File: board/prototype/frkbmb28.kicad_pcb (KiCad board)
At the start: 2 copper layers, 99.1 x 99.1 mm, 175 parts, among them P1 SHITTY_ADD_ON, P2 MCU_CONNECTOR, P3 SCL_JMP, P4 SDA_JMP, U1 IS31FL3741, U2 LIS2HH12

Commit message: ready to start laying out new board
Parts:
- removed R10, R11, R12, R13, R14, R15, R16, R17, R18, R19, R20, R21, R22, R23, R26, R27, R28, R29, R30, R31, R34, R35, R36, R37, R38, R39, R40, R41, R42, R43, R44, R45, R46, R47, R48, R6, R8: R, Resistors_SMD:R_0805_HandSoldering
- removed R7: 100k, Resistors_SMD:R_0603_HandSoldering
- removed R9: 20k, Resistors_SMD:R_0603_HandSoldering
- added C5: 220nF, Capacitors_SMD:C_0603_HandSoldering, F.Cu at (218.7, 121.0)
- added D118: LED, LEDs:LED_0805, F.Cu at (209.9, 163.7)
- added D119: LED, LEDs:LED_0805, F.Cu at (250.5, 127.8)
- added D120: LED, LEDs:LED_0805, F.Cu at (239.7, 161.1)
- added D121: LED, LEDs:LED_0805, F.Cu at (271.7, 127.8)
- added D122: LED, LEDs:LED_0805, F.Cu at (243.9, 155.5)
- added D123: LED, LEDs:LED_0805, F.Cu at (267.5, 133.3)
- added D124: LED, LEDs:LED_0805, F.Cu at (235.4, 166.6)
- added D125: LED, LEDs:LED_0805, F.Cu at (285.4, 116.7)
- added D126: LED, LEDs:LED_0805, F.Cu at (256.7, 144.4)
- added D127: LED, LEDs:LED_0805, F.Cu at (263.2, 127.8)
- added D128: LED, LEDs:LED_0805, F.Cu at (239.7, 150.0)
- added D129: LED, LEDs:LED_0805, F.Cu at (276.3, 122.2)
- added D130: LED, LEDs:LED_0805, F.Cu at (250.5, 138.9)
- added D131: LED, LEDs:LED_0805, F.Cu at (226.9, 162.1)
- added D132: LED, LEDs:LED_0805, F.Cu at (243.9, 144.4)
- added D133: LED, LEDs:LED_0805, F.Cu at (222.7, 167.6)
- added D134: LED, LEDs:LED_0805, F.Cu at (267.8, 122.2)
- added D135: LED, LEDs:LED_0805, F.Cu at (278.8, 111.1)
- added D136: LED, LEDs:LED_0805, F.Cu at (235.4, 155.5)
- added D137: LED, LEDs:LED_0805, F.Cu at (254.7, 133.3)
- added D138: LED, LEDs:LED_0805, F.Cu at (231.2, 161.0)
- added D139: LED, LEDs:LED_0805, F.Cu at (226.9, 167.6)
- added D140: LED, LEDs:LED_0805, F.Cu at (263.2, 133.3)
- added D141: LED, LEDs:LED_0805, F.Cu at (231.2, 166.5)
- added D142: LED, LEDs:LED_0805, F.Cu at (252.4, 144.4)
- added D143: LED, LEDs:LED_0805, F.Cu at (259.0, 138.9)
- added D144: LED, LEDs:LED_0805, F.Cu at (281.1, 116.7)
- C1: value 10uF -> 100nF; footprint SMD_Packages:SMD-1210_Pol -> Capacitors_SMD:C_0603_HandSoldering
- D1, D10, D100, D101, D102, D103, D104, D105, D106, D107, D108, D109, D11, D110, D111, D112, D113, D114, D115, D116, D117, D12, D13, D14, D15, D16, D17, D18, D19, D2, D20, D21, D22, D23, D24, D25, D26, D27, D28, D29, D3, D30, D31, D32, D33, D34, D35, D36, D37, D38, D39, D4, D40, D41, D42, D43, D44, D45, D46, D47, D48, D49, D5, D50, D51, D52, D53, D54, D55, D56, D57, D58, D59, D6, D60, D61, D62, D63, D64, D65, D66, D67, D68, D69, D7, D70, D71, D72, D73, D74, D75, D76, D77, D78, D79, D8, D80, D81, D82, D83, D84, D85, D86, D87, D88, D89, D9, D90, D91, D92, D93, D94, D95, D96, D97, D98, D99: value LED_ARGB -> LED; footprint frkbmb:0606_RGB_COMM_ANODE -> LEDs:LED_0805
- P2: footprint Pin_Headers:Pin_Header_Straight_1x18 -> Pin_Headers:Pin_Header_Straight_1x20
- R1: value R -> 4.7k; footprint Resistors_SMD:R_0805_HandSoldering -> Resistors_SMD:R_0603_HandSoldering
- R2, R3: value 1k -> 4.7k
- R5: value R -> 100k; footprint Resistors_SMD:R_0805_HandSoldering -> Resistors_SMD:R_0603_HandSoldering
- U1: value IS31FL3741 -> IS31FL3731; footprint frkbmb:IS31FL3741 -> frkbmb:IS31FL3731C
- U2: footprint frkbmb:LIS2HH12 -> frkbmb:LIS2HH12-NEW
- moved D19 255.0 mm to (276.9, 116.7)
- moved D21 251.9 mm to (283.1, 111.1)
- moved D22 241.6 mm to (272.0, 122.2)
- moved D101 237.2 mm to (270.3, 111.1)
- moved D110 236.0 mm to (268.4, 116.7)
- moved D109 235.3 mm to (259.0, 133.3)
- moved D73 234.5 mm to (261.8, 111.1)
- moved D20 234.1 mm to (239.7, 155.5)
- moved D112 233.3 mm to (274.6, 111.1)
- moved D100 233.0 mm to (259.3, 122.2)
- moved D83 229.8 mm to (259.9, 116.7)
- moved D23 228.8 mm to (248.2, 150.0)
- moved D78 228.1 mm to (272.6, 116.7)
- moved D96 225.1 mm to (267.5, 127.8)
- moved D91 224.9 mm to (246.2, 133.3)
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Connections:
- C1 pad 1: +3V3 -> GND
- C1 pad 2: GND -> Net-(C1-Pad2)
- C2 pad 1: +3V3 -> GND
- C2 pad 2: GND -> +3V3
- C3 pad 1: +3V3 -> GND
- C3 pad 2: GND -> +3V3
- D1 pad 1: /SW1 -> /CA1
- D1 pad 2: Net-(D1-Pad2) -> /CA2
- D10 pad 1: /SW1 -> /CB1
- D10 pad 2: Net-(D10-Pad2) -> /CB3
- D100 pad 1: /SW1 -> /CA7
- D100 pad 2: Net-(D100-Pad2) -> /CA4
- D101 pad 1: /SW2 -> /CA7
- D101 pad 2: Net-(D100-Pad2) -> /CA5
- D102 pad 1: /SW3 -> /CA7
- D102 pad 2: Net-(D100-Pad2) -> /CA6
- D103 pad 1: /SW4 -> /CA7
- D103 pad 2: Net-(D100-Pad2) -> /CA8
- D104 pad 1: /SW5 -> /CA7
- D104 pad 2: Net-(D100-Pad2) -> /CA9
- D105 pad 1: /SW6 -> /CB7
- D105 pad 2: Net-(D100-Pad2) -> /CB1
- D106 pad 1: /SW7 -> /CB7
- D106 pad 2: Net-(D100-Pad2) -> /CB2
- D107 pad 1: /SW8 -> /CB7
- D107 pad 2: Net-(D100-Pad2) -> /CB3
- D108 pad 1: /SW9 -> /CB7
- D108 pad 2: Net-(D100-Pad2) -> /CB4
- D109 pad 1: /SW1 -> /CB7
- D109 pad 2: Net-(D109-Pad2) -> /CB5
- D11 pad 1: /SW2 -> /CB1
- D11 pad 2: Net-(D10-Pad2) -> /CB4
- D110 pad 1: /SW2 -> /CB7
- D110 pad 2: Net-(D109-Pad2) -> /CB6
- D111 pad 1: /SW3 -> /CB7
- D111 pad 2: Net-(D109-Pad2) -> /CB8
- D112 pad 1: /SW4 -> /CB7
- D112 pad 2: Net-(D109-Pad2) -> /CB9
- D113 pad 1: /SW5 -> /CA8
- D113 pad 2: Net-(D109-Pad2) -> /CA1
- D114 pad 1: /SW6 -> /CA8
- D114 pad 2: Net-(D109-Pad2) -> /CA2
- D115 pad 1: /SW7 -> /CA8
- D115 pad 2: Net-(D109-Pad2) -> /CA3
- D116 pad 1: /SW8 -> /CA8
- D116 pad 2: Net-(D109-Pad2) -> /CA4
- D117 pad 1: /SW9 -> /CA8
- D117 pad 2: Net-(D109-Pad2) -> /CA5
- D12 pad 1: /SW3 -> /CB1
- D12 pad 2: Net-(D10-Pad2) -> /CB5
- D13 pad 1: /SW4 -> /CB1
- D13 pad 2: Net-(D10-Pad2) -> /CB6
- D14 pad 1: /SW5 -> /CB1
- D14 pad 2: Net-(D10-Pad2) -> /CB7
- D15 pad 1: /SW6 -> /CB1
- D15 pad 2: Net-(D10-Pad2) -> /CB8
- D16 pad 1: /SW7 -> /CB1
- D16 pad 2: Net-(D10-Pad2) -> /CB9
- D17 pad 1: /SW8 -> /CA2
- D17 pad 2: Net-(D10-Pad2) -> /CA1
- D18 pad 1: /SW9 -> /CA2
- D18 pad 2: Net-(D10-Pad2) -> /CA3
- D19 pad 1: /SW1 -> /CA2
- D19 pad 2: Net-(D19-Pad2) -> /CA4
- D2 pad 1: /SW2 -> /CA1
- D2 pad 2: Net-(D1-Pad2) -> /CA3
- D20 pad 1: /SW2 -> /CA2
- D20 pad 2: Net-(D19-Pad2) -> /CA5
- D21 pad 1: /SW3 -> /CA2
- D21 pad 2: Net-(D19-Pad2) -> /CA6
- D22 pad 1: /SW4 -> /CA2
- D22 pad 2: Net-(D19-Pad2) -> /CA7
- D23 pad 1: /SW5 -> /CA2
- D23 pad 2: Net-(D19-Pad2) -> /CA8
- D24 pad 1: /SW6 -> /CA2
- D24 pad 2: Net-(D19-Pad2) -> /CA9
- D25 pad 1: /SW7 -> /CB2
- D25 pad 2: Net-(D19-Pad2) -> /CB1
- D26 pad 1: /SW8 -> /CB2
- D26 pad 2: Net-(D19-Pad2) -> /CB3
- D27 pad 1: /SW9 -> /CB2
- D27 pad 2: Net-(D19-Pad2) -> /CB4
- D28 pad 1: /SW1 -> /CB2
- D28 pad 2: Net-(D28-Pad2) -> /CB5
- D29 pad 1: /SW2 -> /CB2
- D29 pad 2: Net-(D28-Pad2) -> /CB6
- D3 pad 1: /SW3 -> /CA1
- D3 pad 2: Net-(D1-Pad2) -> /CA4
- D30 pad 1: /SW3 -> /CB2
- D30 pad 2: Net-(D28-Pad2) -> /CB7
- D31 pad 1: /SW4 -> /CB2
- D31 pad 2: Net-(D28-Pad2) -> /CB8
- D32 pad 1: /SW5 -> /CB2
- D32 pad 2: Net-(D28-Pad2) -> /CB9
- D33 pad 1: /SW6 -> /CA3
- D33 pad 2: Net-(D28-Pad2) -> /CA1
- D34 pad 1: /SW7 -> /CA3
- D34 pad 2: Net-(D28-Pad2) -> /CA2
- D35 pad 1: /SW8 -> /CA3
- D35 pad 2: Net-(D28-Pad2) -> /CA4
- D36 pad 1: /SW9 -> /CA3
- D36 pad 2: Net-(D28-Pad2) -> /CA5
- D37 pad 1: /SW1 -> /CA3
- D37 pad 2: Net-(D37-Pad2) -> /CA6
- D38 pad 1: /SW2 -> /CA3
- D38 pad 2: Net-(D37-Pad2) -> /CA7
- D39 pad 1: /SW3 -> /CA3
- D39 pad 2: Net-(D37-Pad2) -> /CA8
- D4 pad 1: /SW4 -> /CA1
- D4 pad 2: Net-(D1-Pad2) -> /CA5
- D40 pad 1: /SW4 -> /CA3
- D40 pad 2: Net-(D37-Pad2) -> /CA9
- D41 pad 1: /SW5 -> /CB3
- D41 pad 2: Net-(D37-Pad2) -> /CB1
- D42 pad 1: /SW6 -> /CB3
- D42 pad 2: Net-(D37-Pad2) -> /CB2
- D43 pad 1: /SW7 -> /CB3
- D43 pad 2: Net-(D37-Pad2) -> /CB4
- D44 pad 1: /SW8 -> /CB3
- D44 pad 2: Net-(D37-Pad2) -> /CB5
- D45 pad 1: /SW9 -> /CB3
- D45 pad 2: Net-(D37-Pad2) -> /CB6
- D46 pad 1: /SW1 -> /CB3
- D46 pad 2: Net-(D46-Pad2) -> /CB7
- D47 pad 1: /SW2 -> /CB3
- D47 pad 2: Net-(D46-Pad2) -> /CB8
- D48 pad 1: /SW3 -> /CB3
- D48 pad 2: Net-(D46-Pad2) -> /CB9
- D49 pad 1: /SW4 -> /CA4
- D49 pad 2: Net-(D46-Pad2) -> /CA1
- D5 pad 1: /SW5 -> /CA1
- D5 pad 2: Net-(D1-Pad2) -> /CA6
- D50 pad 1: /SW5 -> /CA4
- D50 pad 2: Net-(D46-Pad2) -> /CA2
- D51 pad 1: /SW6 -> /CA4
- D51 pad 2: Net-(D46-Pad2) -> /CA3
- D52 pad 1: /SW7 -> /CA4
- D52 pad 2: Net-(D46-Pad2) -> /CA5
- D53 pad 1: /SW8 -> /CA4
- D53 pad 2: Net-(D46-Pad2) -> /CA6
- D54 pad 1: /SW9 -> /CA4
- D54 pad 2: Net-(D46-Pad2) -> /CA7
- D55 pad 1: /SW1 -> /CA4
- D55 pad 2: Net-(D55-Pad2) -> /CA8
- D56 pad 1: /SW2 -> /CA4
- D56 pad 2: Net-(D55-Pad2) -> /CA9
- D57 pad 1: /SW3 -> /CB4
- D57 pad 2: Net-(D55-Pad2) -> /CB1
- D58 pad 1: /SW4 -> /CB4
- D58 pad 2: Net-(D55-Pad2) -> /CB2
- D59 pad 1: /SW5 -> /CB4
- D59 pad 2: Net-(D55-Pad2) -> /CB3
- D6 pad 1: /SW6 -> /CA1
- D6 pad 2: Net-(D1-Pad2) -> /CA7
- D60 pad 1: /SW6 -> /CB4
- D60 pad 2: Net-(D55-Pad2) -> /CB5
- D61 pad 1: /SW7 -> /CB4
- D61 pad 2: Net-(D55-Pad2) -> /CB6
- D62 pad 1: /SW8 -> /CB4
- D62 pad 2: Net-(D55-Pad2) -> /CB7
- D63 pad 1: /SW9 -> /CB4
- D63 pad 2: Net-(D55-Pad2) -> /CB8
- D64 pad 1: /SW1 -> /CB4
- D64 pad 2: Net-(D64-Pad2) -> /CB9
- D65 pad 1: /SW2 -> /CA5
- D65 pad 2: Net-(D64-Pad2) -> /CA1
- D66 pad 1: /SW3 -> /CA5
- D66 pad 2: Net-(D64-Pad2) -> /CA2
- D67 pad 1: /SW4 -> /CA5
- D67 pad 2: Net-(D64-Pad2) -> /CA3
- D68 pad 1: /SW5 -> /CA5
- D68 pad 2: Net-(D64-Pad2) -> /CA4
- D69 pad 1: /SW6 -> /CA5
- D69 pad 2: Net-(D64-Pad2) -> /CA6
- D7 pad 1: /SW7 -> /CA1
- D7 pad 2: Net-(D1-Pad2) -> /CA8
- D70 pad 1: /SW7 -> /CA5
- D70 pad 2: Net-(D64-Pad2) -> /CA7
- D71 pad 1: /SW8 -> /CA5
- D71 pad 2: Net-(D64-Pad2) -> /CA8
- D72 pad 1: /SW9 -> /CA5
- D72 pad 2: Net-(D64-Pad2) -> /CA9
- D73 pad 1: /SW1 -> /CB5
- D73 pad 2: Net-(D73-Pad2) -> /CB1
- D74 pad 1: /SW2 -> /CB5
- D74 pad 2: Net-(D73-Pad2) -> /CB2
- D75 pad 1: /SW3 -> /CB5
- D75 pad 2: Net-(D73-Pad2) -> /CB3
- D76 pad 1: /SW4 -> /CB5
- D76 pad 2: Net-(D73-Pad2) -> /CB4
- D77 pad 1: /SW5 -> /CB5
- D77 pad 2: Net-(D73-Pad2) -> /CB6
- D78 pad 1: /SW6 -> /CB5
- D78 pad 2: Net-(D73-Pad2) -> /CB7
- D79 pad 1: /SW7 -> /CB5
- D79 pad 2: Net-(D73-Pad2) -> /CB8
- D8 pad 1: /SW8 -> /CA1
- D8 pad 2: Net-(D1-Pad2) -> /CA9
- D80 pad 1: /SW8 -> /CB5
- D80 pad 2: Net-(D73-Pad2) -> /CB9
- D81 pad 1: /SW9 -> /CA6
- D81 pad 2: Net-(D73-Pad2) -> /CA1
- D82 pad 1: /SW1 -> /CA6
- D82 pad 2: Net-(D82-Pad2) -> /CA2
- D83 pad 1: /SW2 -> /CA6
- D83 pad 2: Net-(D82-Pad2) -> /CA3
- D84 pad 1: /SW3 -> /CA6
- D84 pad 2: Net-(D82-Pad2) -> /CA4
- D85 pad 1: /SW4 -> /CA6
- D85 pad 2: Net-(D82-Pad2) -> /CA5
- D86 pad 1: /SW5 -> /CA6
- D86 pad 2: Net-(D82-Pad2) -> /CA7
- D87 pad 1: /SW6 -> /CA6
- D87 pad 2: Net-(D82-Pad2) -> /CA8
- D88 pad 1: /SW7 -> /CA6
- D88 pad 2: Net-(D82-Pad2) -> /CA9
- D89 pad 1: /SW8 -> /CB6
- D89 pad 2: Net-(D82-Pad2) -> /CB1
- D9 pad 1: /SW9 -> /CB1
- D9 pad 2: Net-(D1-Pad2) -> /CB2
- D90 pad 1: /SW9 -> /CB6
- D90 pad 2: Net-(D82-Pad2) -> /CB2
- D91 pad 1: /SW1 -> /CB6
- D91 pad 2: Net-(D91-Pad2) -> /CB3
- D92 pad 1: /SW2 -> /CB6
- D92 pad 2: Net-(D91-Pad2) -> /CB4
- D93 pad 1: /SW3 -> /CB6
- D93 pad 2: Net-(D91-Pad2) -> /CB5
- D94 pad 1: /SW4 -> /CB6
- D94 pad 2: Net-(D91-Pad2) -> /CB7
- D95 pad 1: /SW5 -> /CB6
- D95 pad 2: Net-(D91-Pad2) -> /CB8
- D96 pad 1: /SW6 -> /CB6
- D96 pad 2: Net-(D91-Pad2) -> /CB9
- D97 pad 1: /SW7 -> /CA7
- D97 pad 2: Net-(D91-Pad2) -> /CA1
- D98 pad 1: /SW8 -> /CA7
- D98 pad 2: Net-(D91-Pad2) -> /CA2
- D99 pad 1: /SW9 -> /CA7
- D99 pad 2: Net-(D91-Pad2) -> /CA3
- P2 pad 10: /SCL_ACC -> /AUD
- P2 pad 11: /SA0/SDo -> /SDA_ACC
- P2 pad 12: /CS -> /SCL_ACC
- P2 pad 13: /INT1 -> /SA0/SDo
- P2 pad 14: /INT2 -> /CS
- P2 pad 15: /SDA_SAO -> /INT1
- P2 pad 16: /SCL_SAO -> /INT2
- P2 pad 17: /GPIO1 -> /SDA_SAO
- P2 pad 18: /GPIO2 -> /SCL_SAO
- P2 pad 5: /SDA_MTX -> GND
- P2 pad 6: /SCL_MTX -> /SDA_MTX
- P2 pad 7: /INTB -> /SCL_MTX
- P2 pad 8: /SDB -> /INTB
- P2 pad 9: /SDA_ACC -> /SDB
- R1 pad 1: Net-(D1-Pad2) -> /INTB
- R1 pad 2: /CS1 -> +3V3
- R2 pad 1: +3V3 -> /SCL_MTX
- R2 pad 2: /SCL_MTX -> +3V3
- R3 pad 1: +3V3 -> /SDA_MTX
- R3 pad 2: /SDA_MTX -> +3V3
- R4 pad 1: +3V3 -> GND
- R4 pad 2: /SDB -> Net-(R4-Pad2)
- R5 pad 1: Net-(D1-Pad3) -> GND
- R5 pad 2: /CS2 -> Net-(R5-Pad2)
- U1 pad 1: /CS34 -> /CA9
- U1 pad 10: /SCL_MTX -> Net-(U1-Pad10)
- U1 pad 11: /SDB -> Net-(U1-Pad11)
- U1 pad 12: (no net) -> Net-(U1-Pad12)
- U1 pad 14: +3V3 -> Net-(U1-Pad14)
- U1 pad 15: +3V3 -> Net-(U1-Pad15)
- U1 pad 16: /SW1 -> Net-(C1-Pad2)
- U1 pad 17: /SW2 -> Net-(C5-Pad1)
- U1 pad 18: /SW3 -> GND
- U1 pad 19: /SW4 -> /SDA_MTX
- U1 pad 2: /CS35 -> +3V3
- U1 pad 20: /SW5 -> /SCL_MTX
- U1 pad 21: /SW6 -> /CA1
- U1 pad 22: /SW7 -> /CA2
- U1 pad 23: /SW8 -> /CA3
- U1 pad 24: /SW9 -> /CA4
- U1 pad 25: +3V3 -> /CA5
- U1 pad 26: /CS1 -> /CA6
- U1 pad 27: /CS2 -> /CA7
- U1 pad 28: /CS3 -> /CA8
- U1 pad 29: /CS4 -> GND
- U1 pad 3: /CS36 -> /SDB
- U1 pad 4: /CS37 -> /INTB
- U1 pad 5: /CS38 -> GND
- U1 pad 6: /CS39 -> Net-(R5-Pad2)
- U1 pad 7: /INTB -> Net-(U1-Pad7)
- U1 pad 8: GND -> Net-(U1-Pad8)
- U1 pad 9: /SDA_MTX -> Net-(U1-Pad9)
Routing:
- net Net-(D109-Pad4): track 46.2 -> 0.00 mm, vias 9 -> 0
- net Net-(D100-Pad4): track 45.9 -> 0.00 mm, vias 9 -> 0
- net Net-(D91-Pad4): track 45.8 -> 0.00 mm, vias 9 -> 0
- net Net-(D82-Pad4): track 45.6 -> 0.00 mm, vias 9 -> 0
- net Net-(D73-Pad4): track 45.6 -> 0.00 mm, vias 9 -> 0
- net Net-(D64-Pad4): track 45.3 -> 0.00 mm, vias 9 -> 0
- net Net-(D55-Pad4): track 45.1 -> 0.00 mm, vias 9 -> 0
- net Net-(D46-Pad4): track 45.0 -> 0.00 mm, vias 9 -> 0
- net Net-(D37-Pad4): track 44.8 -> 0.00 mm, vias 9 -> 0
- net Net-(D28-Pad4): track 44.7 -> 0.00 mm, vias 9 -> 0
- net Net-(D1-Pad4): track 44.6 -> 0.00 mm, vias 9 -> 0
- net Net-(D19-Pad4): track 44.5 -> 0.00 mm, vias 9 -> 0
- net Net-(D10-Pad4): track 44.4 -> 0.00 mm, vias 9 -> 0
- net /SW7: track 39.8 -> 0.00 mm
- net /SW9: track 39.6 -> 0.00 mm
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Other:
- board outline removed
- net class Default: trace_width 0.2 -> 0.127
- rule pad_to_mask_clearance: 0.2 -> 0
- rule trace_min: 0.2 -> 0.127
- rule via_min_size: 0.45 -> 0.4

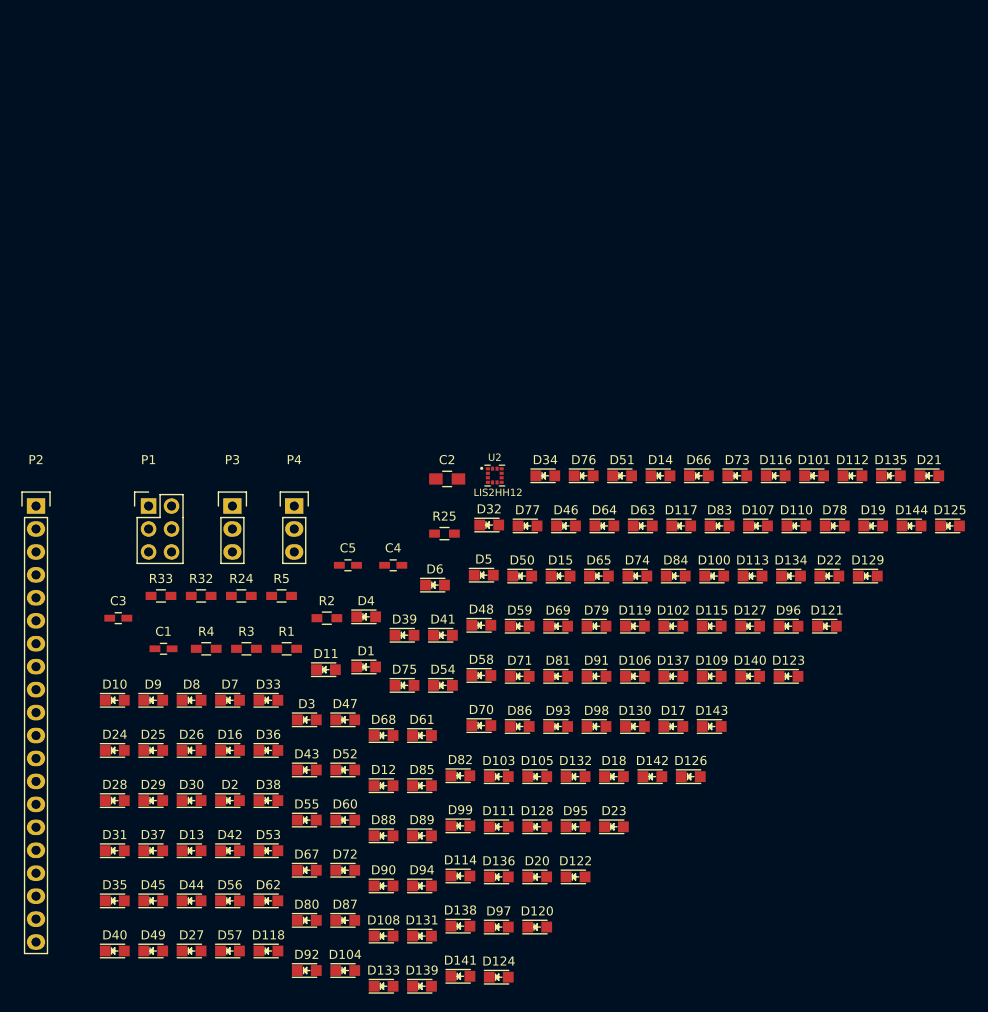
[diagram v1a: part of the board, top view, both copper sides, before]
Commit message: organized the LEDs on the prototype
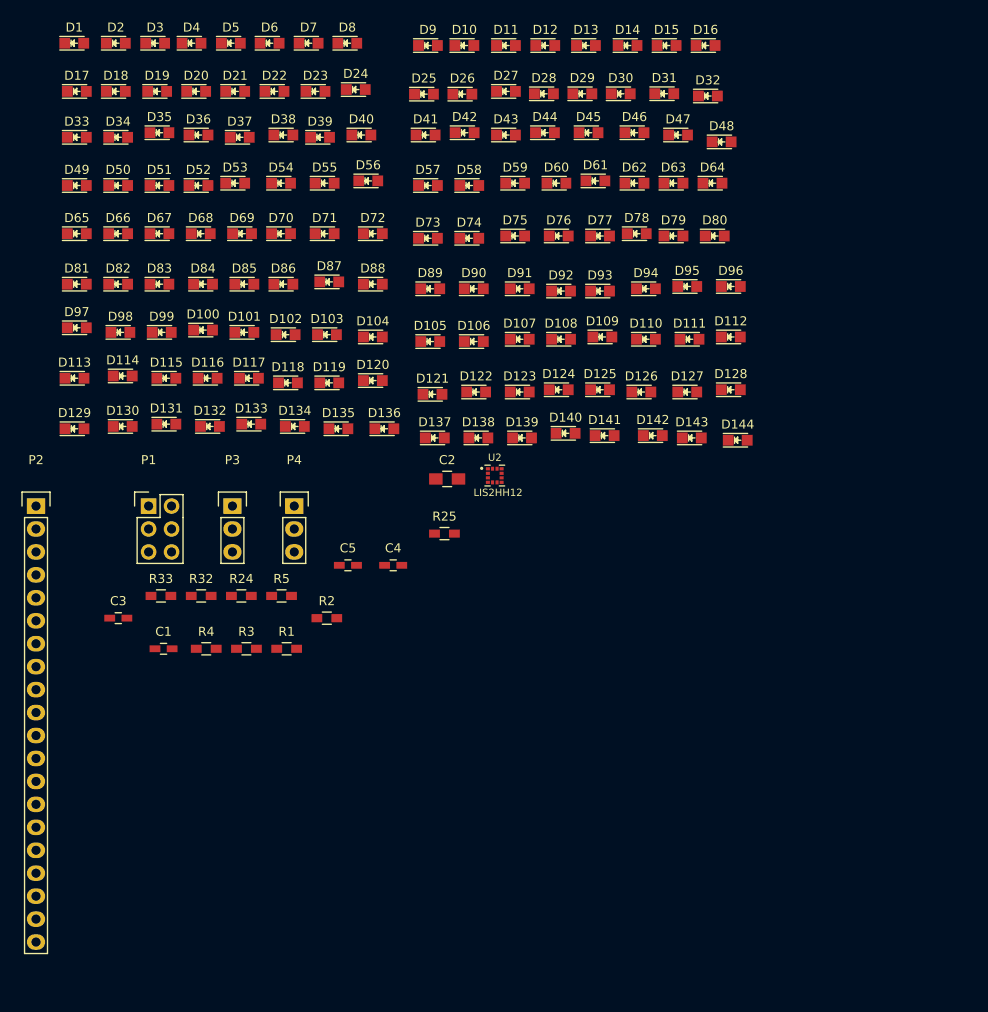
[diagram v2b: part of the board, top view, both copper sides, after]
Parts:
- moved D31 103.5 mm to (253.7, 68.8)
- moved D27 101.3 mm to (236.2, 68.6)
- moved D13 99.2 mm to (245.1, 63.5)
- moved D45 97.7 mm to (245.4, 73.2)
- moved D17 96.4 mm to (188.7, 68.6)
- moved D20 94.8 mm to (201.9, 68.6)
- moved D40 94.4 mm to (220.2, 73.4)
- moved D16 94.1 mm to (258.3, 63.5)
- moved D18 93.8 mm to (193.0, 68.6)
- moved D44 93.6 mm to (240.5, 73.2)
- moved D19 92.7 mm to (197.6, 68.6)
- moved D28 91.5 mm to (240.4, 68.8)
- moved D29 91.5 mm to (244.7, 68.8)
- moved D30 91.5 mm to (248.9, 68.8)
- moved D129 89.3 mm to (188.5, 105.9)
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
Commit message: ready to export gerbers, waiting on approval from group
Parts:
- added G***: LOGO, frkbmb:MATOKO_SMALL, F.Cu at (172.4, 95.6)
- added G***: LOGO, frkbmb:safety_first, F.Cu at (173.4, 68.6)
- added G***: LOGO, frkbmb:sig, F.Cu at (161.0, 116.5)
- moved U2 115.8 mm to (119.3, 116.5), turned to 180 degrees
- moved D25 111.2 mm to (117.3, 86.1)
- moved D57 111.0 mm to (117.3, 92.1)
- moved D121 110.8 mm to (117.3, 104.1)
- moved D89 110.8 mm to (117.3, 98.1)
- moved D58 109.6 mm to (123.3, 92.1)
- moved D122 109.6 mm to (123.3, 104.1)
- moved D90 109.6 mm to (123.3, 98.1)
- moved D26 109.4 mm to (123.3, 86.1)
- moved D9 109.0 mm to (120.3, 83.1)
- moved D59 108.7 mm to (129.3, 92.1)
- moved D91 108.7 mm to (129.3, 98.1)
- moved D123 108.4 mm to (129.3, 104.1)
- moved D27 108.3 mm to (129.3, 86.1)
- moved D41 108.2 mm to (120.3, 89.1)
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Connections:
- P2 pad 13: /SA0/SDo -> /SA0_SDO
- R32 pad 2: /SAO/SDO -> /SA0_SDO
- R4 pad 2: Net-(R4-Pad2) -> /SDB
- U1 pad 10: Net-(U1-Pad10) -> /CB4
- U1 pad 11: Net-(U1-Pad11) -> /CB5
- U1 pad 12: Net-(U1-Pad12) -> /CB6
- U1 pad 13: Net-(U1-Pad13) -> /CB7
- U1 pad 14: Net-(U1-Pad14) -> /CB8
- U1 pad 15: Net-(U1-Pad15) -> /CB9
- U1 pad 7: Net-(U1-Pad7) -> /CB1
- U1 pad 8: Net-(U1-Pad8) -> /CB2
- U1 pad 9: Net-(U1-Pad9) -> /CB3
- U2 pad 3: /SAO/SDO -> /SA0_SDO
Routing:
- net GND: track 4.17 -> 403.4 mm, vias 0 -> 49
- net /CA5: track 0.00 -> 193.3 mm, vias 0 -> 9
- net /CA3: track 0.00 -> 182.5 mm, vias 0 -> 8
- net /CA4: track 0.00 -> 182.4 mm, vias 0 -> 8
- net /CA2: track 0.00 -> 160.9 mm, vias 0 -> 8
- net /CA6: track 0.00 -> 156.1 mm, vias 0 -> 9
- net /CA7: track 0.00 -> 148.4 mm, vias 0 -> 9
- net /CA8: track 0.00 -> 144.1 mm, vias 0 -> 9
- net /CA9: track 0.00 -> 140.0 mm, vias 0 -> 9
- net /CA1: track 0.00 -> 136.7 mm, vias 0 -> 8
- net +3V3: track 0.00 -> 108.1 mm, vias 0 -> 4
- net /CB1: track 0.00 -> 107.1 mm, vias 0 -> 11
- net /CB2: track 0.00 -> 100.8 mm, vias 0 -> 10
- net /CB8: track 0.00 -> 94.1 mm, vias 0 -> 8
- net /CB6: track 0.00 -> 93.9 mm, vias 0 -> 8
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- added copper zone on B.Cu, net GND
- added copper zone on F.Cu, net GND
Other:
- board outline added: 70 x 92 mm
- net class Default: clearance 0.127 -> 0.203; trace_width 0.127 -> 0.19
- rule trace_clearance: 0.127 -> 0.203
- rule trace_min: 0.127 -> 0.19
- rule via_min_size: 0.4 -> 0
- board text added: "3V3+"
- board text added: "ACC"
- board text added: "AUD"
- board text added: "CS"
- board text added: "GND"
- board text added: "GPIO1"
- board text added: "GPIO2"
- board text added: "INT1"
- board text added: "INT2"
- board text added: "INTB"
- board text added: "IS31FL3731"
- board text added: "MATRIX"
- board text added: "MCU HEADER"
- board text added: "MTX"
- board text added: "POWER"
- board text added: "SA0/ SDO"
- board text added: "SAO"
- board text added: "SCL"
- board text added: "SDA"
- board text added: "SDB"
- board text added: "SHITTY ADD-ON"
- board text added: "frkbmb type0"
- board text added: "safety first with android girls"

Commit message: wired power and LED matrix
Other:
- board text added: "JLCJLCJLCJLC"
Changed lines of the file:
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@@
     (area 112.399999 50.539999 182.500001 142.640001)
     (thickness 1.6)
-    (drawings 72)
+    (drawings 73)
     (tracks 1483)
     (zones 0)
@@
     (visible_elements FFFFFF7F)
     (pcbplotparams
-      (layerselection 0x00030_80000001)
+      (layerselection 0x010f0_80000001)
       (usegerberextensions false)
       (excludeedgelayer true)
@@
       (outputformat 1)
       (mirror false)
-      (drillshape 1)
+      (drillshape 0)
       (scaleselection 1)
-      (outputdirectory ""))
+      (outputdirectory gerbers/))
   )
   (net 0 "")
@@
     (pad "" smd rect (at 0 0 90) (size 2 1) (layers F.Cu F.Paste F.Mask))
   )
+  (gr_text JLCJLCJLCJLC (at 180.34 130.81 90) (layer B.SilkS)
+    (effects (font (size 1.5 1.5) (thickness 0.3)) (justify mirror))
+  )
   (dimension 71 (width 0.3) (layer Cmts.User)
